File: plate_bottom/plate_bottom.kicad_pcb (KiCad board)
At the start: 2 copper layers, 180.6 x 117.9 mm, 13 parts

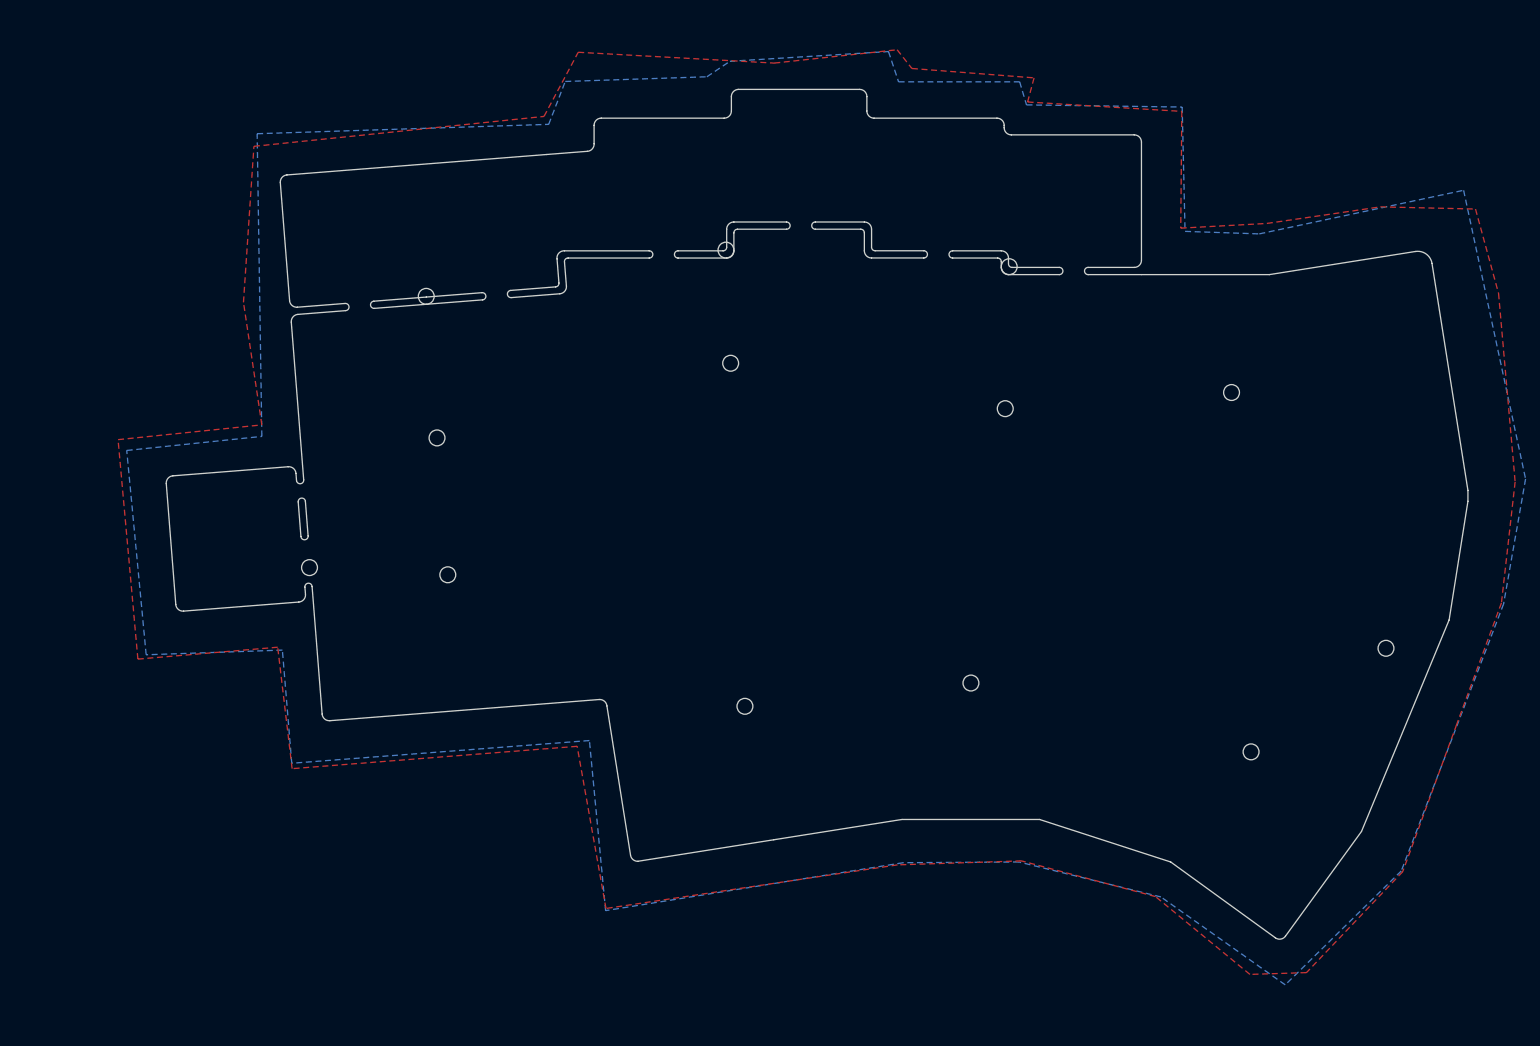
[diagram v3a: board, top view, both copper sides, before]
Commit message: Removed copper layers from top and bottom plates
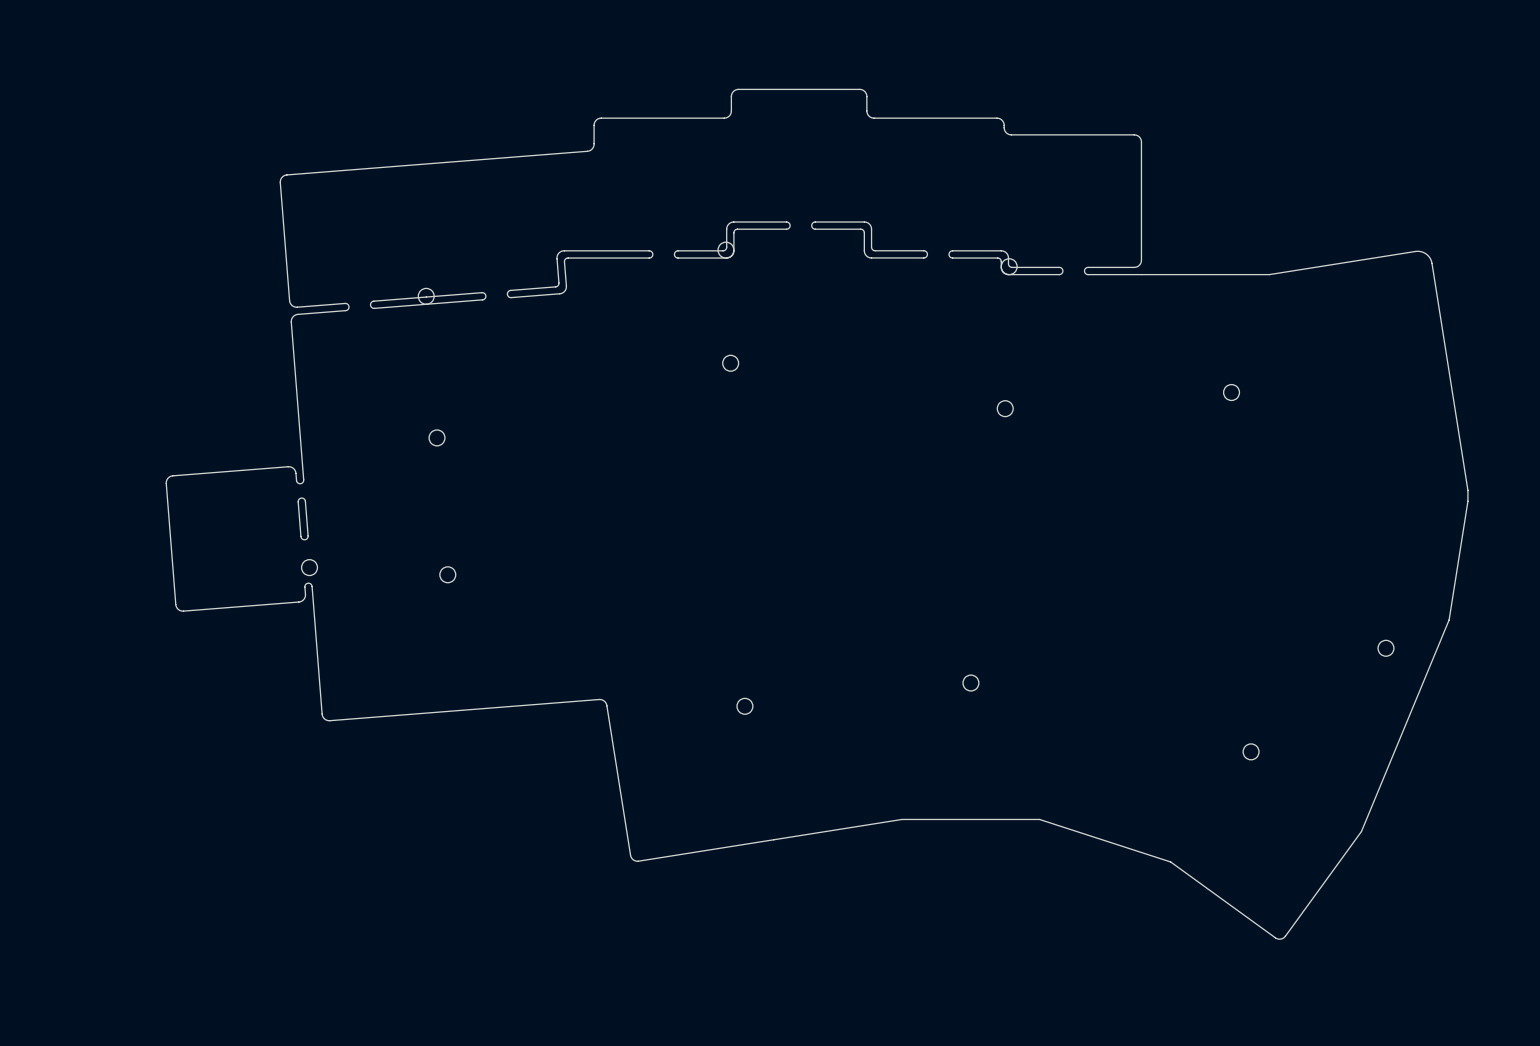
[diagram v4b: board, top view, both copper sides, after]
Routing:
- removed copper zone on B.Cu, net (none)
- removed copper zone on F.Cu, net (none)
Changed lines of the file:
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@@
     (arrow2b (pts (xy 57.05 30.55) (xy 57.636421 31.676504)))
   )
-  (zone (net 0) (net_name "") (layer F.Cu) (hatch edge 0.508)
-    (connect_pads (clearance 0.508))
-    (min_thickness 0.254)
-    (fill yes (arc_segments 32) (thermal_gap 0.508) (thermal_bridge_width 0.508))
-    (polygon
-      (pts
-        (xy 177.8 27.65) (xy 194.75 28.95) (xy 193.85 32.3) (xy 215.25 33.6) (xy 215.1 49.8)
-        (xy 227.05 49.15) (xy 242.8 46.85) (xy 256 47.15) (xy 259.2 58.85) (xy 261.5 85)
-        (xy 259.6 101.8) (xy 253.4 118.65) (xy 245.9 139.1) (xy 232.55 153.1) (xy 224.7 153.35)
-        (xy 211.6 142.55) (xy 193 137.6) (xy 175.8 138.15) (xy 135.35 144.2) (xy 131.35 121.7)
-        (xy 91.8 124.8) (xy 89.8 107.95) (xy 70.4 109.6) (xy 67.65 79.15) (xy 87.6 77.1)
-        (xy 85.05 60.1) (xy 86.5 38.45) (xy 126.75 34.3) (xy 131.5 25.4) (xy 158.7 26.9)
-        (xy 175.75 25.05)
-      )
-    )
-  )
-  (zone (net 0) (net_name "") (layer B.Cu) (hatch edge 0.508)
-    (connect_pads (clearance 0.508))
-    (min_thickness 0.254)
-    (fill yes (arc_segments 32) (thermal_gap 0.508) (thermal_bridge_width 0.508))
-    (polygon
-      (pts
-        (xy 175.95 29.5) (xy 192.75 29.5) (xy 193.7 32.7) (xy 215.3 33) (xy 215.7 50.25)
-        (xy 226 50.6) (xy 254.35 44.55) (xy 262.95 84.6) (xy 259.9 101.95) (xy 245.7 139)
-        (xy 229.6 154.8) (xy 212.35 142.6) (xy 192.65 137.75) (xy 176.6 137.85) (xy 135.3 144.5)
-        (xy 133.05 120.9) (xy 91.75 124.05) (xy 90.45 108.35) (xy 71.55 109) (xy 68.85 80.65)
-        (xy 87.6 78.7) (xy 86.95 36.7) (xy 127.4 35.4) (xy 129.7 29.45) (xy 149.35 28.8)
-        (xy 152.55 26.65) (xy 174.55 25.3)
-      )
-    )
-  )
 )

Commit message: Plates
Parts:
- added HM14: CaseHole, used_footprints:M2_HOLE_PCB, F.Cu at (178.4, 120.5)
- moved HM3 54.4 mm to (196.3, 135.0), turned to 352.5 degrees
- moved HM4 28.4 mm to (157.7, 110.6), turned to 348 degrees
- moved HM5 28.2 mm to (75.0, 76.2), turned to 352.5 degrees
- moved HM6 26.0 mm to (93.5, 81.2), turned to 352.5 degrees
- moved HM8 23.0 mm to (96.0, 62.3), turned to 352.5 degrees
- moved H16 22.3 mm to (205.2, 87.0), turned to 348 degrees
- moved HM13 21.8 mm to (135.4, 105.8), turned to 342 degrees
- moved HM7 20.2 mm to (98.6, 42.8), turned to 352.5 degrees
- moved HM10 16.8 mm to (174.0, 74.7), turned to 348 degrees
- moved HM11 16.6 mm to (138.0, 60.7), turned to 348 degrees
- moved HM9 13.7 mm to (140.6, 45.2), turned to 348 degrees
- moved HM2 12.7 mm to (178.6, 55.6), turned to 2.5 degrees
- moved HM1 11.0 mm to (216.6, 115.2), turned to 340.5 degrees
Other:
- board size 180.6 x 117.9 mm -> 173.5 x 138.9 mm

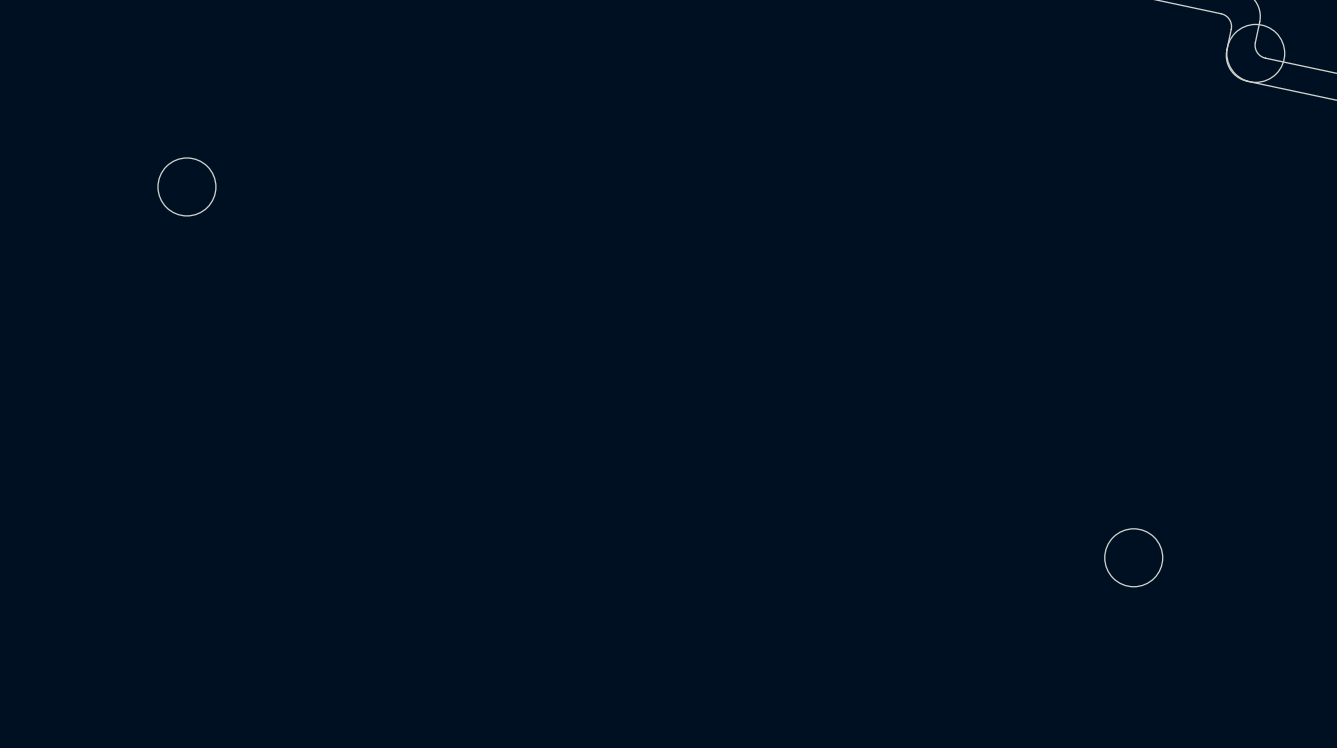
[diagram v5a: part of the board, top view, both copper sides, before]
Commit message: Moved two mounting holes a bit
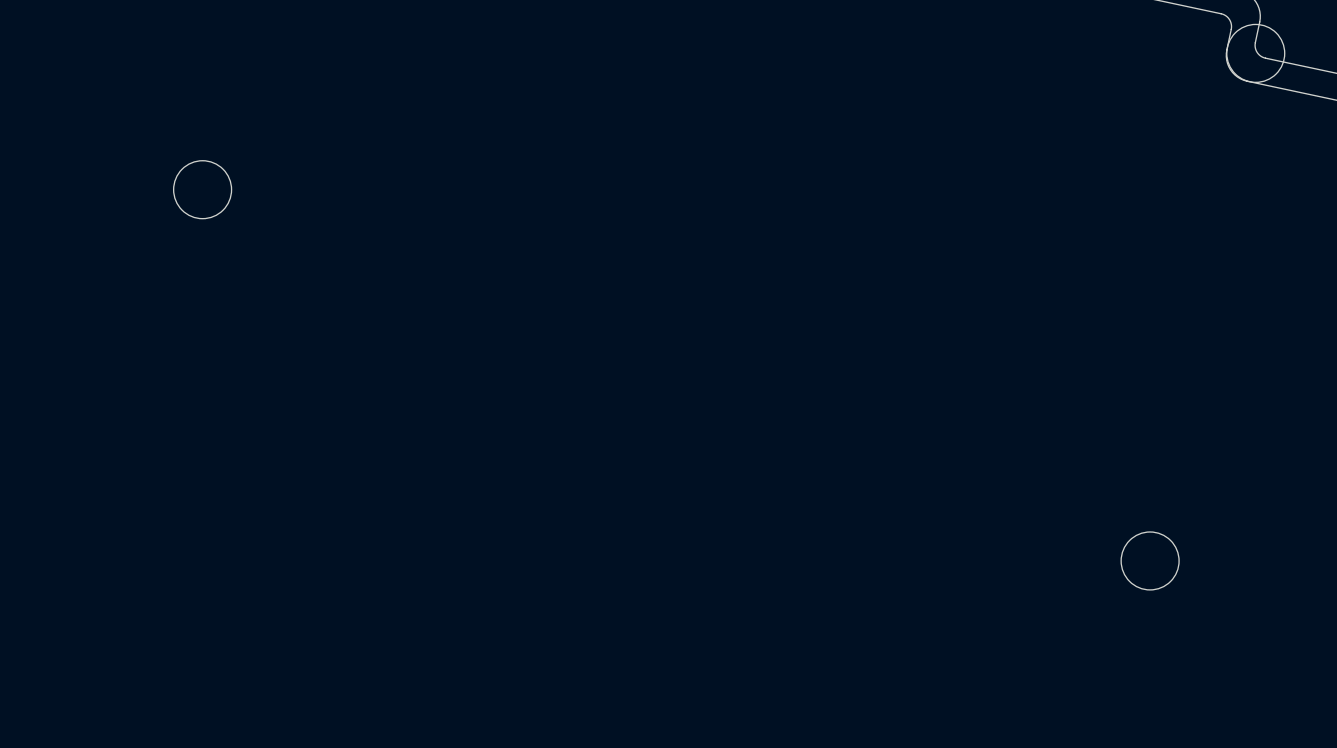
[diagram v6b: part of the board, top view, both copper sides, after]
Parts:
- moved HM10 0.63 mm to (174.6, 74.9)
- moved HM11 0.60 mm to (138.6, 60.8)
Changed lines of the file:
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@@
   (general
     (thickness 1.6)
-    (drawings 144)
+    (drawings 142)
     (tracks 0)
     (zones 0)
@@
     (mod_text_size 1 1)
     (mod_text_width 0.15)
-    (pad_size 4 4)
+    (pad_size 2.2 2.2)
     (pad_drill 2.2)
     (pad_to_mask_clearance 0)
@@
   )
   (module used_footprints:M2_HOLE_PCB (layer F.Cu)
+    (at 138.606105 60.769332 348)
+    (fp_text reference HM11 (at 0 2.7 168) (layer F.SilkS) hide
+      (effects (font (size 1 1) (thickness 0.15)))
+    )
+    (fp_text value CaseHole (at 0 -2.6 168) (layer F.Fab) hide
+      (effects (font (size 1 1) (thickness 0.15)))
+    )
+    (pad "" np_thru_hole circle (at 0 0 348) (size 2.2 2.2) (drill 2.2) (layers *.Cu *.Mask))
+  )
+  (module used_footprints:M2_HOLE_PCB (layer F.Cu)
+    (at 174.590949 74.869116 348)
+    (fp_text reference HM10 (at 0 2.7 168) (layer F.SilkS) hide
+      (effects (font (size 1 1) (thickness 0.15)))
+    )
+    (fp_text value CaseHole (at 0 -2.6 168) (layer F.Fab) hide
+      (effects (font (size 1 1) (thickness 0.15)))
+    )
+    (pad "" np_thru_hole circle (at 0 0 348) (size 2.2 2.2) (drill 2.2) (layers *.Cu *.Mask))
+  )
+  (module used_footprints:M2_HOLE_PCB (layer F.Cu)
     (at 135.411461 105.81821 342)
     (fp_text reference HM13 (at 0 2.7 162) (layer F.SilkS) hide
@@
   )
   (module used_footprints:M2_HOLE_PCB (layer F.Cu)
-    (at 138.011567 60.664674 348)
-    (fp_text reference HM11 (at 0 2.7 168) (layer F.SilkS) hide
-      (effects (font (size 1 1) (thickness 0.15)))
-    )
-    (fp_text value CaseHole (at 0 -2.6 168) (layer F.Fab) hide
-      (effects (font (size 1 1) (thickness 0.15)))
-    )
-    (pad "" np_thru_hole circle (at 0 0 348) (size 2.2 2.2) (drill 2.2) (layers *.Cu *.Mask))
-  )
-  (module used_footprints:M2_HOLE_PCB (layer F.Cu)
     (at 157.667251 110.630611 348)
     (fp_text reference HM4 (at 0 2.7 168) (layer F.SilkS) hide
-      (effects (font (size 1 1) (thickness 0.15)))
-    )
-    (fp_text value CaseHole (at 0 -2.6 168) (layer F.Fab) hide
-      (effects (font (size 1 1) (thickness 0.15)))
-    )
-    (pad "" np_thru_hole circle (at 0 0 348) (size 2.2 2.2) (drill 2.2) (layers *.Cu *.Mask))
-  )
-  (module used_footprints:M2_HOLE_PCB (layer F.Cu)
-    (at 173.969161 74.74843 348)
-    (fp_text reference HM10 (at 0 2.7 168) (layer F.SilkS) hide
       (effects (font (size 1 1) (thickness 0.15)))
     )
@@
   (gr_circle (center 74.958497 76.225236) (end 77.02188 76.66383) (layer Cmts.User) (width 0.15))
   (gr_circle (center 95.998102 62.325863) (end 98.061514 62.764462) (layer Cmts.User) (width 0.15))
-  (gr_circle (center 137.964742 60.644482) (end 140.028155 61.083082) (layer Cmts.User) (width 0.15))
-  (gr_circle (center 173.937738 74.751982) (end 176.001129 75.19057) (layer Cmts.User) (width 0.15))
   (gr_line (start 200.502193 41.443556) (end 200.502214 78.513558) (layer Cmts.User) (width 0.15))
   (gr_line (start 210.906185 150.113866) (end 226.042184 138.503538) (layer Edge.Cuts) (width 0.05))

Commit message: WIP
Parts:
- moved H16 0.58 mm to (204.6, 87.0)
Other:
- outline, holes or cut-outs redrawn
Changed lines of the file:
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@@
   (general
     (thickness 1.6)
-    (drawings 142)
+    (drawings 146)
     (tracks 0)
     (zones 0)
@@
   )
   (module used_footprints:M2_HOLE_PCB (layer F.Cu)
+    (at 204.566053 86.954833 348)
+    (fp_text reference H16 (at 0 2.7 168) (layer F.SilkS) hide
+      (effects (font (size 1 1) (thickness 0.15)))
+    )
+    (fp_text value MountingHole (at 0 -2.6 168) (layer F.Fab) hide
+      (effects (font (size 1 1) (thickness 0.15)))
+    )
+    (pad "" np_thru_hole circle (at 0 0 348) (size 2.2 2.2) (drill 2.2) (layers *.Cu *.Mask))
+  )
+  (module used_footprints:M2_HOLE_PCB (layer F.Cu)
     (at 138.606105 60.769332 348)
     (fp_text reference HM11 (at 0 2.7 168) (layer F.SilkS) hide
@@
   )
   (module used_footprints:M2_HOLE_PCB (layer F.Cu)
-    (at 205.15 86.97 348)
-    (fp_text reference H16 (at 0 2.7 168) (layer F.SilkS) hide
-      (effects (font (size 1 1) (thickness 0.15)))
-    )
-    (fp_text value MountingHole (at 0 -2.6 168) (layer F.Fab) hide
-      (effects (font (size 1 1) (thickness 0.15)))
-    )
-    (pad "" np_thru_hole circle (at 0 0 348) (size 2.2 2.2) (drill 2.2) (layers *.Cu *.Mask))
-  )
-  (module used_footprints:M2_HOLE_PCB (layer F.Cu)
     (at 96.005913 62.32559 352.5)
     (fp_text reference HM8 (at 0 2.7 172.5) (layer F.SilkS) hide
@@
     (pad "" np_thru_hole circle (at 0 0 352.5) (size 2.2 2.2) (drill 2.2) (layers *.Cu *.Mask))
   )
-  (gr_line (start 229.192195 112.403559) (end 226.042189 114.823552) (layer Edge.Cuts) (width 0.05))
+  (gr_line (start 208.566053 86.954833) (end 204.566053 86.954833) (layer Dwgs.User) (width 0.15))
+  (gr_line (start 204.566053 86.954833) (end 207.083336 83.846249) (layer Dwgs.User) (width 0.15))
+  (gr_line (start 200.502338 78.513367) (end 208.562328 85.043358) (layer Cmts.User) (width 0.15))
+  (gr_line (start 206.166304 83.103653) (end 208.046999 84.626605) (layer Dwgs.User) (width 0.15))
+  (gr_line (start 208.562328 85.043358) (end 208.562348 100.723351) (layer Cmts.User) (width 0.15))
+  (gr_line (start 229.192203 62.463549) (end 229.192213 133.929713) (layer Edge.Cuts) (width 0.05))
+  (gr_arc (start 225.217361 134.12252) (end 227.489505 137.389626) (angle -57.95998997) (layer Edge.Cuts) (width 0.05))
+  (gr_line (start 226.042183 138.503528) (end 227.489505 137.389626) (layer Edge.Cuts) (width 0.05))
+  (gr_line (start 210.906185 150.113866) (end 226.042183 138.503528) (layer Edge.Cuts) (width 0.05))
   (gr_arc (start 74.844825 62.938767) (end 75.836298 63.069274) (angle -90) (layer Edge.Cuts) (width 0.05))
   (gr_arc (start 83.089839 23.295806) (end 83.220347 22.304323) (angle -90) (layer Edge.Cuts) (width 0.05))
@@
   (gr_line (start 177.657997 117.537863) (end 181.455814 119.919517) (layer Cmts.User) (width 0.15))
   (gr_line (start 133.650411 103.521887) (end 137.603496 103.922534) (layer Cmts.User) (width 0.15))
-  (gr_line (start 226.042184 138.503538) (end 226.042189 114.823552) (layer Edge.Cuts) (width 0.05))
   (gr_line (start 200.502214 78.513558) (end 208.562196 85.043555) (layer Cmts.User) (width 0.15))
   (gr_line (start 184.27219 146.713548) (end 243.53014 87.444815) (layer Cmts.User) (width 0.15))
@@
   (gr_circle (center 196.327555 134.972524) (end 198.437073 134.972529) (layer Cmts.User) (width 0.15))
   (gr_circle (center 216.622195 115.210934) (end 218.731722 115.210926) (layer Cmts.User) (width 0.15))
-  (gr_circle (center 205.15 86.97) (end 207.259457 86.97) (layer Cmts.User) (width 0.15))
   (gr_circle (center 157.667251 110.630611) (end 159.730651 111.069202) (layer Cmts.User) (width 0.15))
   (gr_circle (center 135.411461 105.81821) (end 137.474862 106.256801) (layer Cmts.User) (width 0.15))
@@
   (gr_arc (start 153.475915 44.425009) (end 153.579888 43.93594) (angle -180) (layer Edge.Cuts) (width 0.05))
   (gr_arc (start 149.56334 43.593355) (end 149.459367 44.082441) (angle -180) (layer Edge.Cuts) (width 0.05))
-  (gr_line (start 229.192205 62.463555) (end 229.192195 112.403559) (layer Edge.Cuts) (width 0.05))
   (gr_line (start 210.906185 150.113866) (end 196.727977 160.995954) (layer Edge.Cuts) (width 0.05))
   (gr_arc (start 227.206792 62.467147) (end 229.192205 62.463555) (angle -92.64101847) (layer Edge.Cuts) (width 0.05))
@@
   (gr_circle (center 95.998102 62.325863) (end 98.061514 62.764462) (layer Cmts.User) (width 0.15))
   (gr_line (start 200.502193 41.443556) (end 200.502214 78.513558) (layer Cmts.User) (width 0.15))
-  (gr_line (start 210.906185 150.113866) (end 226.042184 138.503538) (layer Edge.Cuts) (width 0.05))
   (gr_line (start 196.272191 131.903545) (end 199.402205 135.113547) (layer Cmts.User) (width 0.15))
   (gr_arc (start 171.277986 52.298331) (end 171.381949 51.809242) (angle -180) (layer Edge.Cuts) (width 0.05))

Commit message: Multiple fixes
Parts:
- added SW1: SW_Push, used_footprints:bumpon_mark, F.Cu at (87.9, 30.6)
- added SW10: SW_Push, used_footprints:bumpon_mark, F.Cu at (146.8, 51.2)
- added SW12: SW_Push, used_footprints:bumpon_mark, F.Cu at (217.3, 67.8)
- added SW12: SW_Push, used_footprints:bumpon_mark, F.Cu at (182.8, 65.3)
- added SW19: SW_Push, used_footprints:bumpon_mark, F.Cu at (217.4, 109.3)
- added SW20: SW_Push, used_footprints:bumpon_mark, F.Cu at (80.4, 87.3)
- added SW27: SW_Push, used_footprints:bumpon_mark, F.Cu at (63.7, 68.2)
- added SW28: SW_Push, used_footprints:bumpon_mark, F.Cu at (121.7, 110.9)
- added SW30: SW_Push, used_footprints:bumpon_mark, F.Cu at (162.5, 119.9)
- added SW32: SW_Push, used_footprints:bumpon_mark, F.Cu at (195.2, 146.3)
- added SW4: SW_Push, used_footprints:bumpon_mark, F.Cu at (150.8, 32.5)
- added SW6: SW_Push, used_footprints:bumpon_mark, F.Cu at (186.8, 46.6)
- added SW7: SW_Push, used_footprints:bumpon_mark, F.Cu at (85.4, 49.5)
- moved HM1 6.44 mm to (222.7, 117.2)
- moved HM10 3.24 mm to (172.1, 72.7)
- moved HM11 3.24 mm to (136.2, 58.6)
- moved HM6 3.24 mm to (91.1, 79.1)
- moved HM4 3.24 mm to (155.2, 108.5)
- moved HM7 3.24 mm to (96.2, 40.7)
- moved HM13 3.24 mm to (133.0, 103.7)
- moved HM2 3.24 mm to (176.2, 53.5)
- moved HM9 3.24 mm to (138.2, 43.0)
- moved HM3 3.24 mm to (193.9, 132.8)
- moved HM8 3.24 mm to (93.6, 60.2)
- moved HM14 3.24 mm to (176.0, 118.4)
- moved HM5 3.24 mm to (72.5, 74.1)
- moved H16 2.72 mm to (202.1, 85.9)
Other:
- outline, holes or cut-outs redrawn
